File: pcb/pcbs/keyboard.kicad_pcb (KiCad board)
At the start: 2 copper layers, 152.4 x 110.9 mm, 97 parts, among them J1 Jumper, J10 Jumper, J11 Jumper, J12 Jumper, J13 Jumper, J14 Jumper, J15 Jumper, J16 Jumper, J17 Jumper, J18 Jumper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

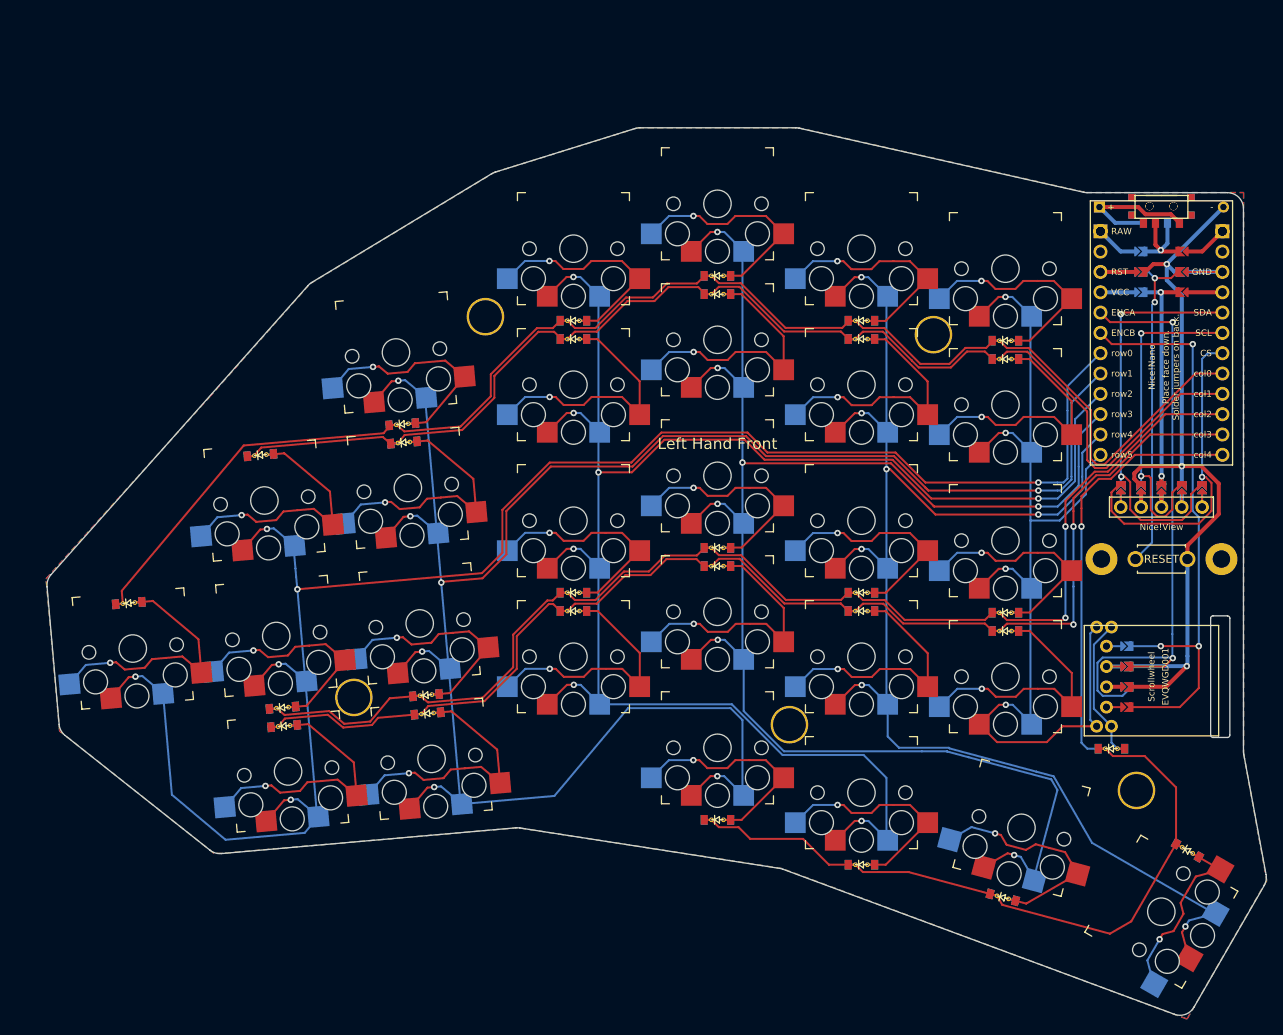
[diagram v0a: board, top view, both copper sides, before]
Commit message: fixed some drc problems Squashed commit of the following:
commit fc0171f96f06824f930dc5825498fa5e5ecf1060
Author: daniel <github@dbauer.me>
Date:   Tue Jul 18 11:26:57 2023 +0200

    reversible slider

commit 837158be306a0aa2e166f52b0d32387ab34f280f
Author: daniel <github@dbauer.me>
Date:   Tue Jul 18 10:56:47 2023 +0200

    make hole footprints plated
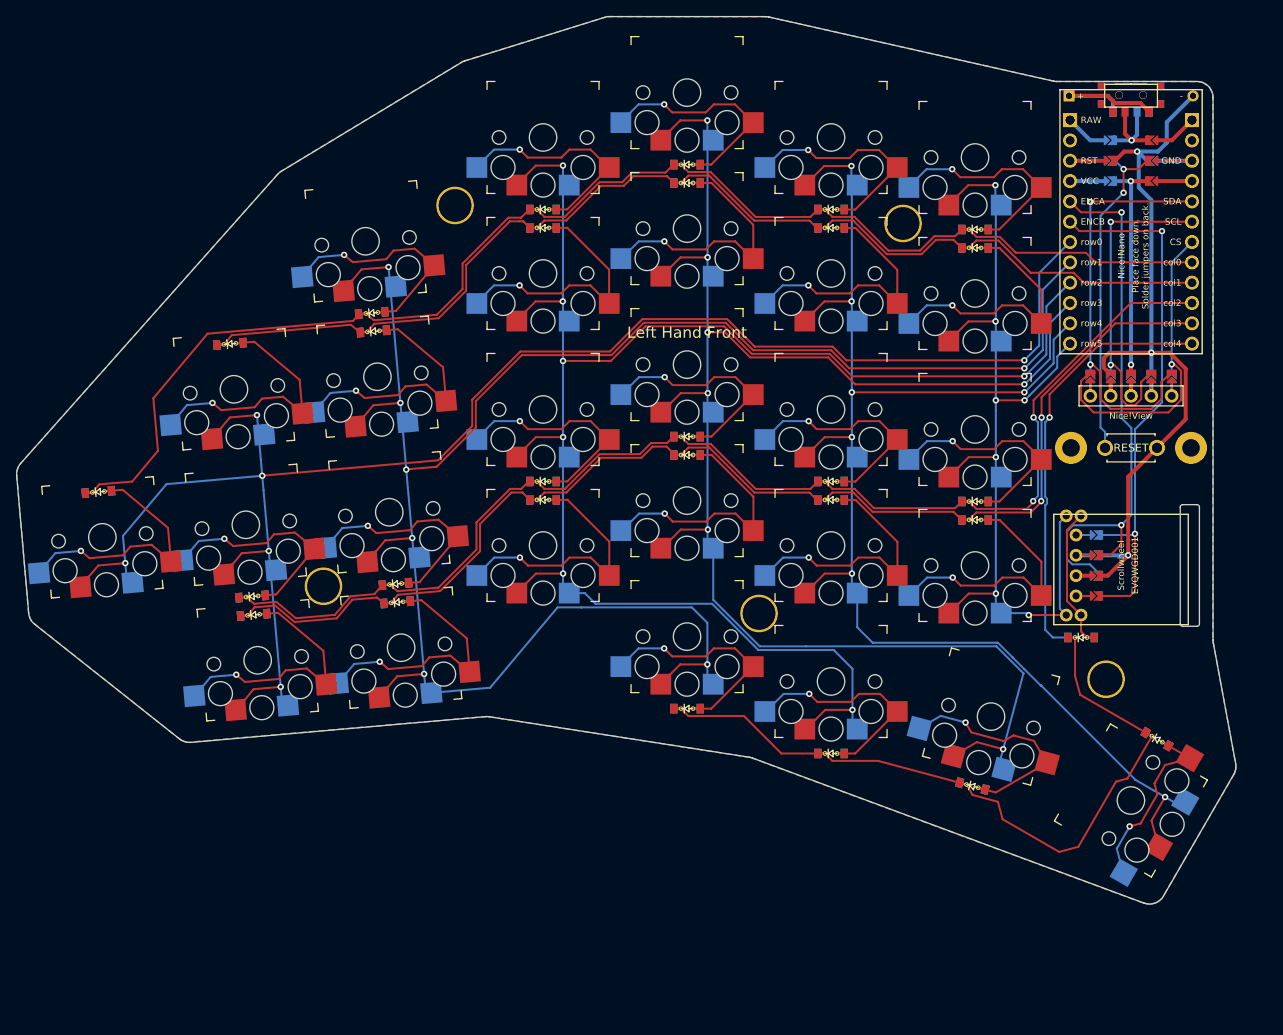
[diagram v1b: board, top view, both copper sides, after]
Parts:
- removed the ? at (121.1, 81.3) (x2)
- removed the S20 at (139.1, 90.9)
- removed S24: , PG1350
- removed T2: , E73:SPDT_C128955
- added ? (x2): , lib:text, F.Cu at (117.3, 67.4)
- added S20: , PG1350, F.Cu at (135.3, 77.0)
- added S20: , PG1350, F.Cu at (153.3, 79.5)
- moved J3 14.4 mm to (168.5, 97.8)
- moved J5 14.4 mm to (168.5, 97.8)
- moved S13 14.4 mm to (117.3, 105.4)
- moved _4 14.4 mm to (88.3, 51.5)
- moved D29 14.4 mm to (166.5, 105.5)
- moved S11 14.4 mm to (99.3, 60.0)
- moved _6 14.4 mm to (71.8, 99.1)
- moved J16 14.4 mm to (170.2, 72.8)
- moved J23 14.4 mm to (170.2, 72.8)
- moved J10 14.4 mm to (175.3, 45.9)
- moved J12 14.4 mm to (175.3, 45.9)
- moved S9 14.4 mm to (99.3, 94.0)
- moved Nice!View1 14.4 mm to (172.8, 75.3)
- moved S23 14.4 mm to (153.3, 96.5)
- moved D12 14.4 mm to (153.3, 88.5)
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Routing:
- net row0: track 229.3 -> 215.9 mm
- net row5: track 128.8 -> 117.3 mm, vias 4 -> 7
- net col1: track 159.3 -> 148.0 mm
- net row1: track 253.1 -> 242.4 mm
- net col0: track 186.5 -> 176.2 mm
- net ENCA: track 75.4 -> 68.3 mm
- net row4: track 183.1 -> 176.5 mm
- net ENCB: track 73.2 -> 67.2 mm, vias 3 -> 2
- net row2: track 218.9 -> 213.1 mm
- net row3: track 210.4 -> 206.2 mm
- net GND: track 96.0 -> 92.3 mm
- net col4: track 146.4 -> 150.0 mm
- net RST: track 40.8 -> 41.9 mm
- net col3: track 161.9 -> 160.9 mm
- net CS: track 41.2 -> 40.2 mm
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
